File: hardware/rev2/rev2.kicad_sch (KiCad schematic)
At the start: 31 parts, among them J2 SMA, J3 SMA, J4 Antenna RF and GNSS Data, J5 Antenna GND, J7 USB_C_Receptacle_USB2.0_16P, U4 EClamp2522P

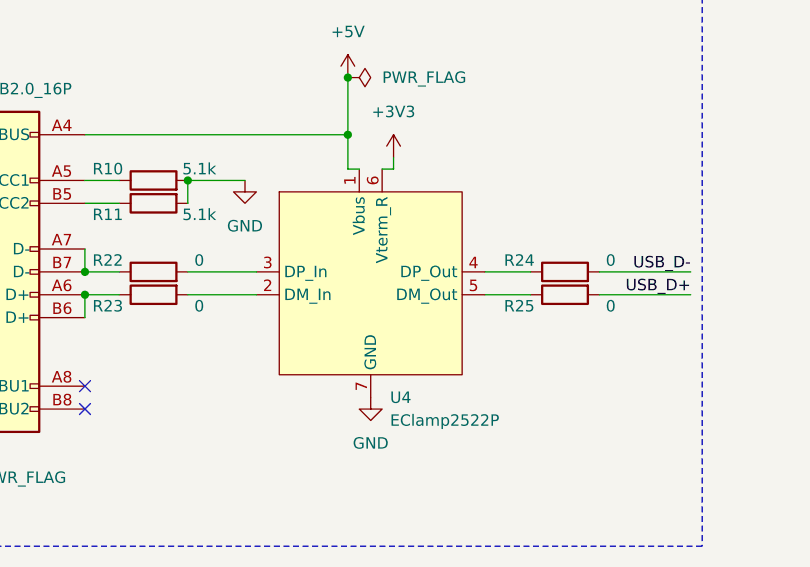
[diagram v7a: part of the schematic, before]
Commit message: set all applicable components for sx1262
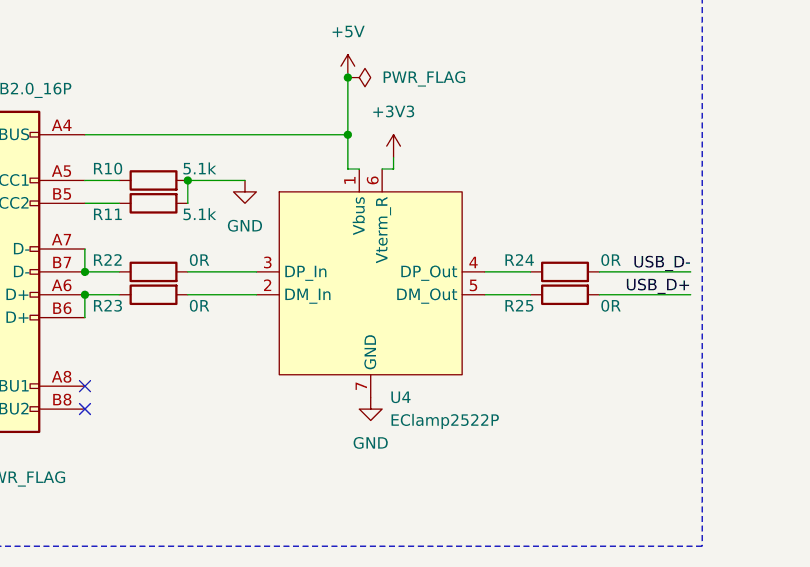
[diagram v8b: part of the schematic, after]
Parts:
- R22, R23, R24, R25: value 0 -> 0R; footprint Inductor_SMD:L_0603_1608Metric_Pad1.05x0.95mm_HandSolder -> Resistor_SMD:R_0603_1608Metric_Pad0.98x0.95mm_HandSolder
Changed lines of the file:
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@@
 			)
 		)
-		(property "Value" "0"
+		(property "Value" "0R"
 			(at 59.69 71.12 90)
 			(show_name no)
@@
 			)
 		)
-		(property "Footprint" "Inductor_SMD:L_0603_1608Metric_Pad1.05x0.95mm_HandSolder"
+		(property "Footprint" "Resistor_SMD:R_0603_1608Metric_Pad0.98x0.95mm_HandSolder"
 			(at 54.61 74.168 90)
 			(hide yes)
@@
 			)
 		)
-		(property "Value" "0"
+		(property "Value" "0R"
 			(at 59.69 76.2 90)
 			(show_name no)
@@
 			)
 		)
-		(property "Footprint" "Inductor_SMD:L_0603_1608Metric_Pad1.05x0.95mm_HandSolder"
+		(property "Footprint" "Resistor_SMD:R_0603_1608Metric_Pad0.98x0.95mm_HandSolder"
 			(at 54.61 73.152 90)
 			(hide yes)
@@
 			)
 		)
-		(property "Value" "0"
+		(property "Value" "0R"
 			(at 105.41 76.2 90)
 			(show_name no)
@@
 			)
 		)
-		(property "Footprint" "Inductor_SMD:L_0603_1608Metric_Pad1.05x0.95mm_HandSolder"
+		(property "Footprint" "Resistor_SMD:R_0603_1608Metric_Pad0.98x0.95mm_HandSolder"
 			(at 100.33 73.152 90)
 			(hide yes)
@@
 			)
 		)
-		(property "Value" "0"
+		(property "Value" "0R"
 			(at 105.41 71.12 90)
 			(show_name no)
@@
 			)
 		)
-		(property "Footprint" "Inductor_SMD:L_0603_1608Metric_Pad1.05x0.95mm_HandSolder"
+		(property "Footprint" "Resistor_SMD:R_0603_1608Metric_Pad0.98x0.95mm_HandSolder"
 			(at 100.33 74.168 90)
 			(hide yes)
